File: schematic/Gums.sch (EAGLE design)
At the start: 36 parts, among them IC3 74LS595N, IC4 74LS595N, U1 ATMEGA328P_PDIP

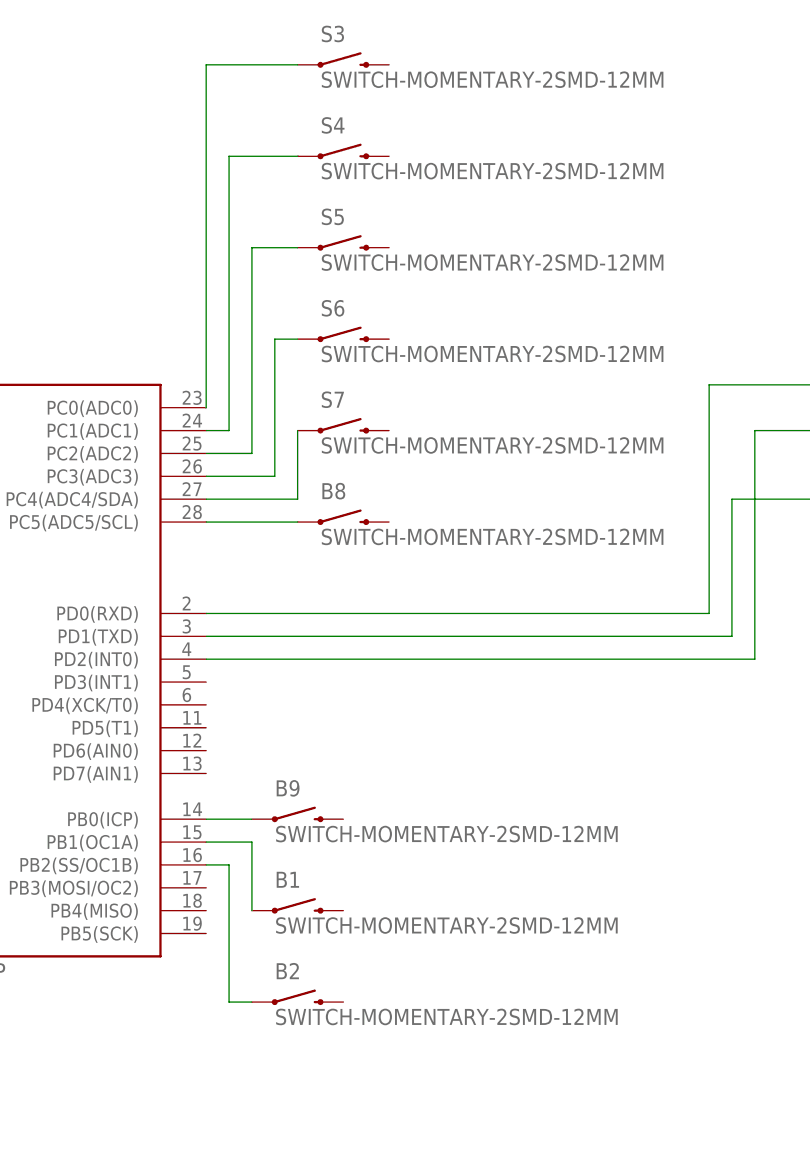
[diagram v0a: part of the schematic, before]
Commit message: Updated the schematic with ground on the switches.
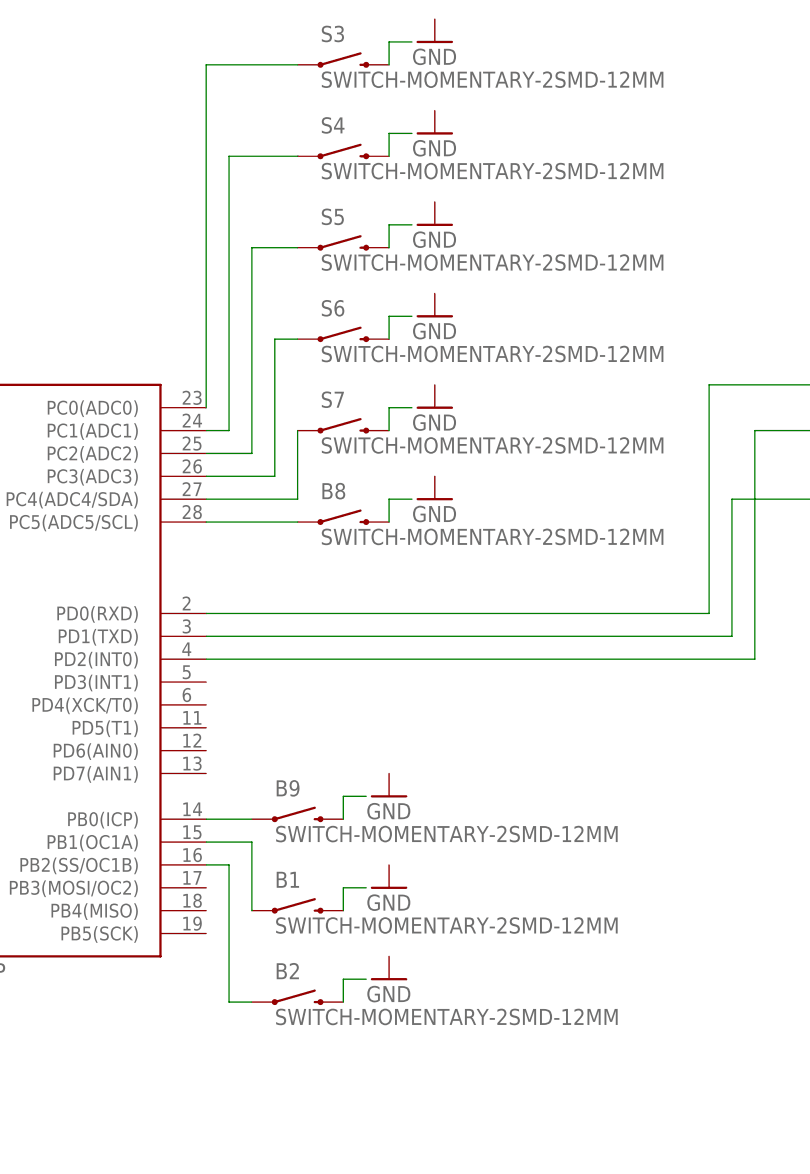
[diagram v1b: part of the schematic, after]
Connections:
- new net N$38: S3.2
- new net N$39: S4.2
- new net N$40: S5.2
- new net N$41: S6.2
- new net N$42: S7.2
- new net N$43: B8.2
- new net N$44: B9.2
- new net N$45: B1.2
- new net N$46: B2.2
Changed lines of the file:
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@@
 <setting verticaltext="up"/>
 </settings>
-<grid distance="0.1" unitdist="inch" unit="inch" style="dots" multiple="1" display="yes" altdistance="0.01" altunitdist="inch" altunit="inch"/>
+<grid distance="0.1" unitdist="inch" unit="inch" style="lines" multiple="1" display="no" altdistance="0.01" altunitdist="inch" altunit="inch"/>
 <layers>
 <layer number="1" name="Top" color="4" fill="1" visible="no" active="no"/>
@@
 <part name="D12" library="SparkFun-LED" deviceset="LED" device="5MM"/>
 <part name="GND4" library="SparkFun-Aesthetics" deviceset="GND" device=""/>
+<part name="GND5" library="SparkFun-Aesthetics" deviceset="GND" device=""/>
+<part name="GND6" library="SparkFun-Aesthetics" deviceset="GND" device=""/>
+<part name="GND7" library="SparkFun-Aesthetics" deviceset="GND" device=""/>
+<part name="GND8" library="SparkFun-Aesthetics" deviceset="GND" device=""/>
+<part name="GND9" library="SparkFun-Aesthetics" deviceset="GND" device=""/>
+<part name="GND10" library="SparkFun-Aesthetics" deviceset="GND" device=""/>
+<part name="GND11" library="SparkFun-Aesthetics" deviceset="GND" device=""/>
+<part name="GND12" library="SparkFun-Aesthetics" deviceset="GND" device=""/>
+<part name="GND13" library="SparkFun-Aesthetics" deviceset="GND" device=""/>
 </parts>
 <sheets>
@@
 <instance part="D12" gate="G$1" x="210.82" y="17.78" rot="R90"/>
 <instance part="GND4" gate="1" x="220.98" y="10.16"/>
+<instance part="GND5" gate="1" x="86.36" y="132.08"/>
+<instance part="GND6" gate="1" x="86.36" y="121.92"/>
+<instance part="GND7" gate="1" x="86.36" y="111.76"/>
+<instance part="GND8" gate="1" x="86.36" y="101.6"/>
+<instance part="GND9" gate="1" x="86.36" y="91.44"/>
+<instance part="GND10" gate="1" x="86.36" y="81.28"/>
+<instance part="GND11" gate="1" x="81.28" y="48.26"/>
+<instance part="GND12" gate="1" x="81.28" y="38.1"/>
+<instance part="GND13" gate="1" x="81.28" y="27.94"/>
 </instances>
 <busses>
@@
 </segment>
 </net>
+<net name="N$38" class="0">
+<segment>
+<pinref part="S3" gate="G$1" pin="2"/>
+<wire x1="81.28" y1="129.54" x2="81.28" y2="132.08" width="0.1524" layer="91"/>
+<wire x1="81.28" y1="132.08" x2="83.82" y2="132.08" width="0.1524" layer="91"/>
+</segment>
+</net>
+<net name="N$39" class="0">
+<segment>
+<pinref part="S4" gate="G$1" pin="2"/>
+<wire x1="81.28" y1="119.38" x2="81.28" y2="121.92" width="0.1524" layer="91"/>
+<wire x1="81.28" y1="121.92" x2="83.82" y2="121.92" width="0.1524" layer="91"/>
+</segment>
+</net>
+<net name="N$40" class="0">
+<segment>
+<pinref part="S5" gate="G$1" pin="2"/>
+<wire x1="81.28" y1="109.22" x2="81.28" y2="111.76" width="0.1524" layer="91"/>
+<wire x1="81.28" y1="111.76" x2="83.82" y2="111.76" width="0.1524" layer="91"/>
+</segment>
+</net>
+<net name="N$41" class="0">
+<segment>
+<pinref part="S6" gate="G$1" pin="2"/>
+<wire x1="81.28" y1="99.06" x2="81.28" y2="101.6" width="0.1524" layer="91"/>
+<wire x1="81.28" y1="101.6" x2="83.82" y2="101.6" width="0.1524" layer="91"/>
+</segment>
+</net>
+<net name="N$42" class="0">
+<segment>
+<pinref part="S7" gate="G$1" pin="2"/>
+<wire x1="81.28" y1="88.9" x2="81.28" y2="91.44" width="0.1524" layer="91"/>
+<wire x1="81.28" y1="91.44" x2="83.82" y2="91.44" width="0.1524" layer="91"/>
+</segment>
+</net>
+<net name="N$43" class="0">
+<segment>
+<pinref part="B8" gate="G$1" pin="2"/>
+<wire x1="81.28" y1="78.74" x2="81.28" y2="81.28" width="0.1524" layer="91"/>
+<wire x1="81.28" y1="81.28" x2="83.82" y2="81.28" width="0.1524" layer="91"/>
+</segment>
+</net>
+<net name="N$44" class="0">
+<segment>
+<pinref part="B9" gate="G$1" pin="2"/>
+<wire x1="76.2" y1="45.72" x2="76.2" y2="48.26" width="0.1524" layer="91"/>
+<wire x1="76.2" y1="48.26" x2="78.74" y2="48.26" width="0.1524" layer="91"/>
+</segment>
+</net>
+<net name="N$45" class="0">
+<segment>
+<pinref part="B1" gate="G$1" pin="2"/>
+<wire x1="76.2" y1="35.56" x2="76.2" y2="38.1" width="0.1524" layer="91"/>
+<wire x1="76.2" y1="38.1" x2="78.74" y2="38.1" width="0.1524" layer="91"/>
+</segment>
+</net>
+<net name="N$46" class="0">
+<segment>
+<pinref part="B2" gate="G$1" pin="2"/>
+<wire x1="76.2" y1="25.4" x2="76.2" y2="27.94" width="0.1524" layer="91"/>
+<wire x1="76.2" y1="27.94" x2="78.74" y2="27.94" width="0.1524" layer="91"/>
+</segment>
+</net>

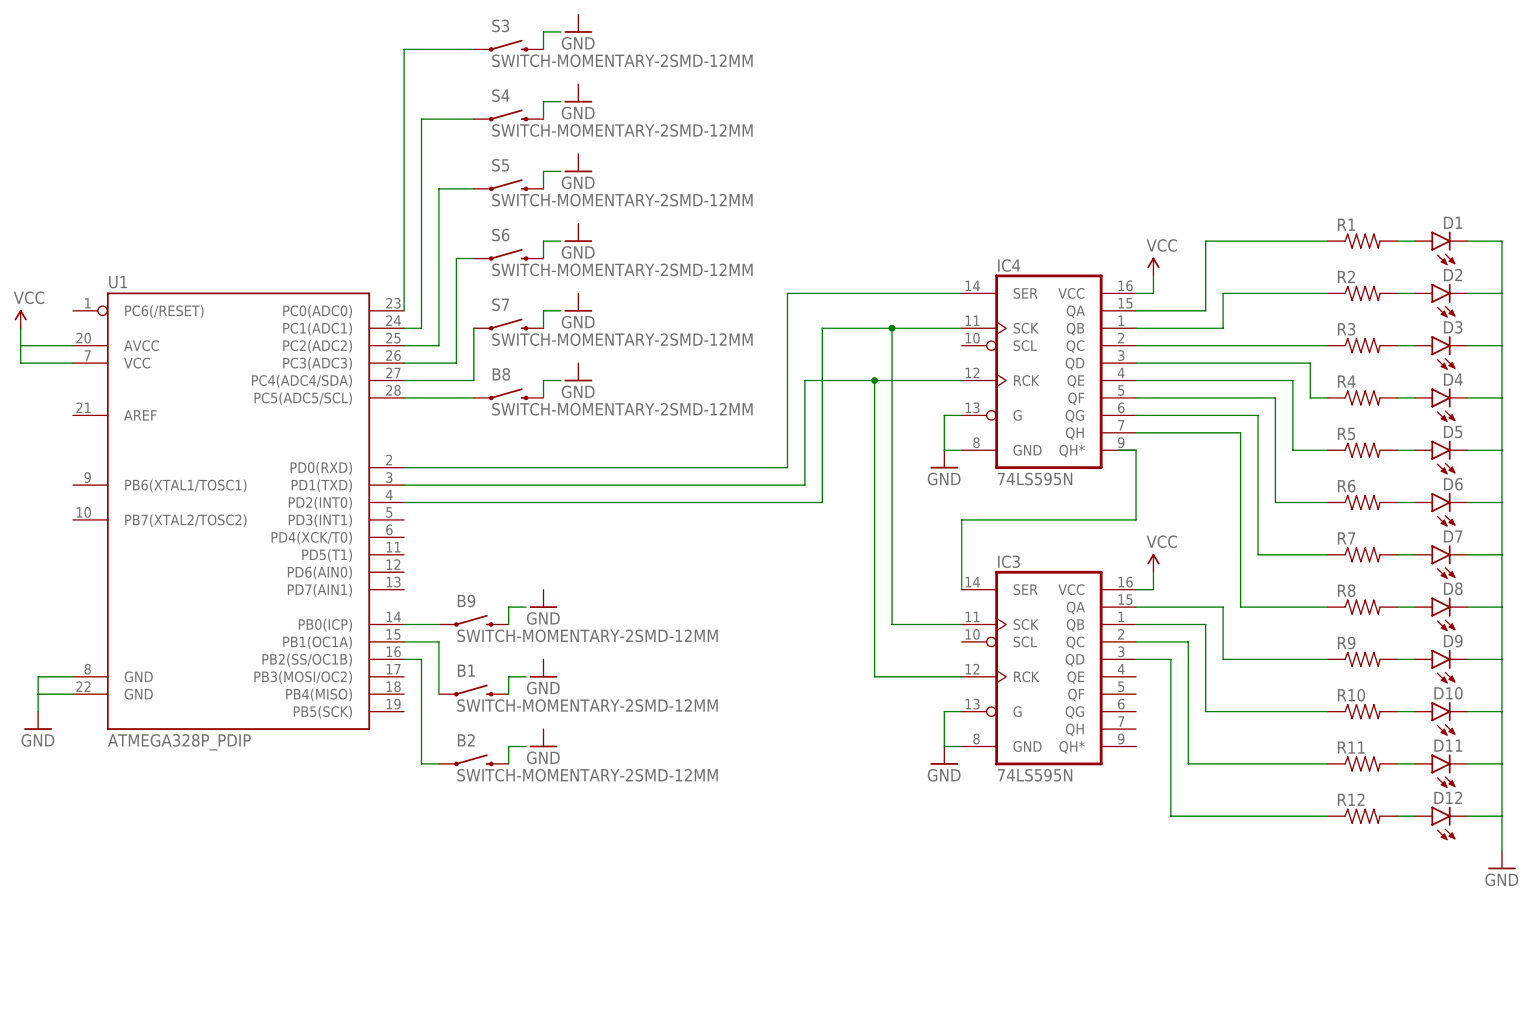
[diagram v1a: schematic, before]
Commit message: Updated the schematic to include three more leds (so can have 5-digit guessables).
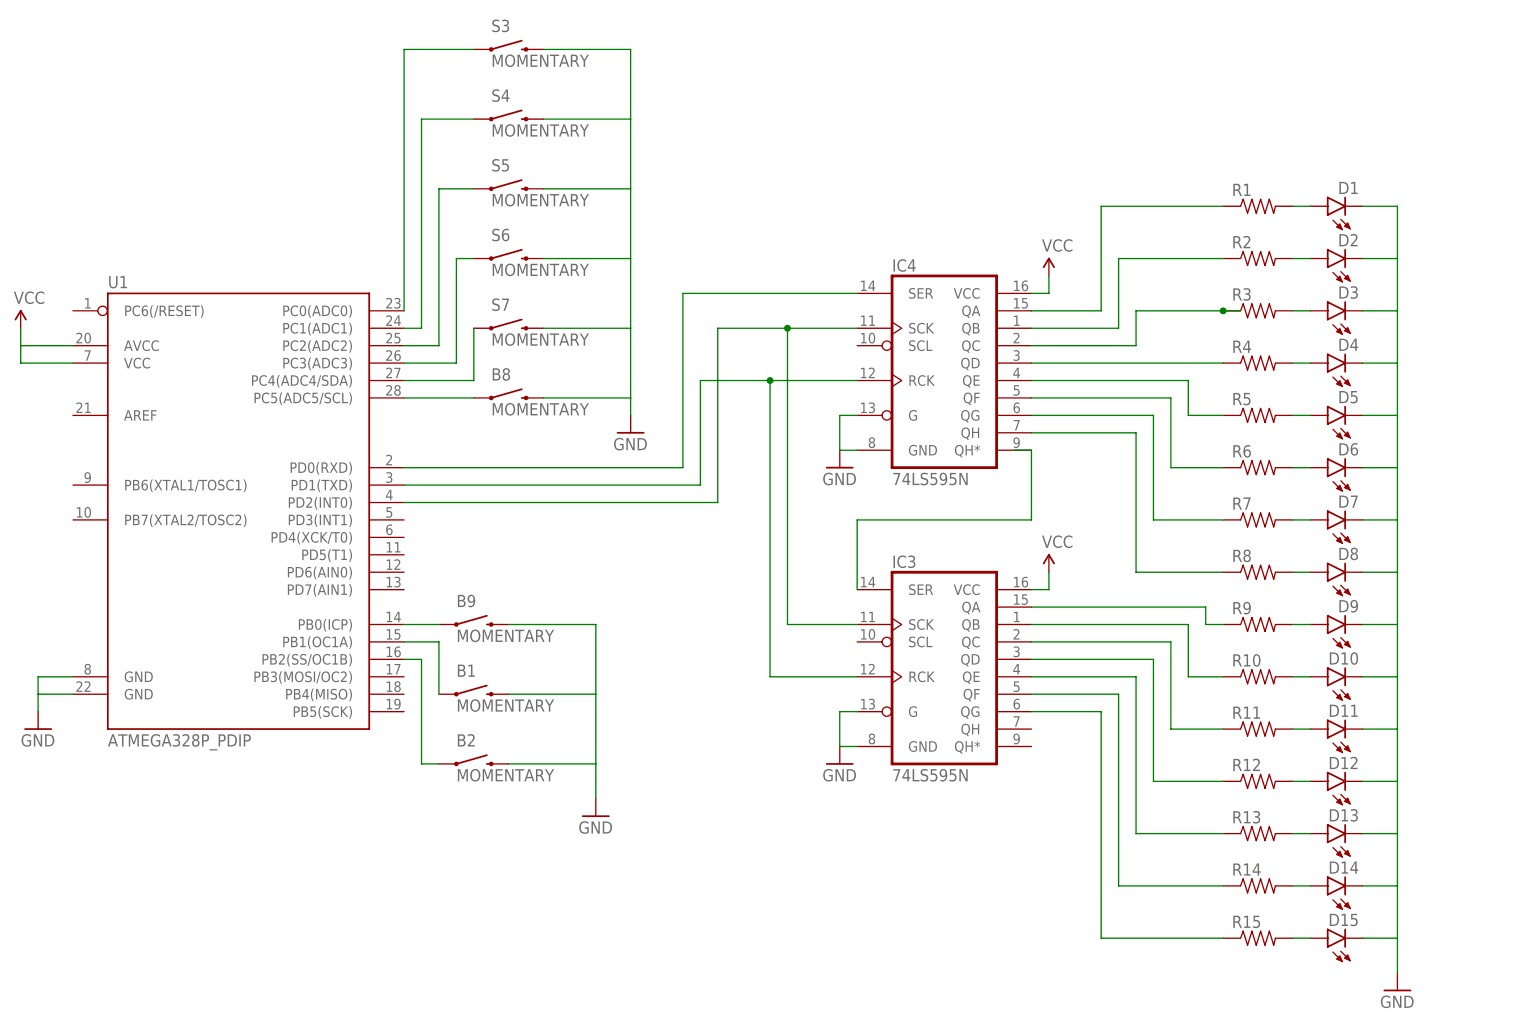
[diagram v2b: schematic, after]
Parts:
- added D13, D14, D15: (no value), SparkFun-LED:LED5MM
- added R13, R14, R15: (no value), SparkFun-Resistors:RESISTORPTH-1/4W
- B1, B2, B8, B9, S3, S4, S5, S6, S7: value SWITCH-MOMENTARY-2SMD-12MM -> MOMENTARY
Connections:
- removed net N$38: S3.2
- removed net N$39: S4.2
- removed net N$40: S5.2
- removed net N$41: S6.2
- removed net N$42: S7.2
- removed net N$43: B8.2
- removed net N$44: B9.2
- removed net N$45: B1.2
- removed net N$46: B2.2
- new net N$47: D13.A, R13.2
- new net N$48: D14.A, R14.2
- new net N$49: D15.A, R15.2
- new net N$50: IC3.QE, R13.1
- new net N$51: IC3.QF, R14.1
- new net N$52: IC3.QG, R15.1
- net GND: now also B1.2, B2.2, B8.2, B9.2, D13.C, D14.C, D15.C, S3.2, S4.2, S5.2, S6.2, S7.2
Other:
- moved on the sheet: D1, D10, D11, D12, D2, D3, D4, D5, D6, D7, D8, D9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
